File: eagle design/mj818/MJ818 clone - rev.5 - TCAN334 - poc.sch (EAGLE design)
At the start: 6 parts, among them J1 CAN, J2 Power Supply, J3 LED

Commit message: MJ818: confirmed pulldown resistor for rear LED PWM line (driver input side) is needed
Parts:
- removed R102: 10k, rcl:R-EU_R0402
- renumbered J1 to J103, J2 to J101, J3 to J102
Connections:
- removed net DIM_REAR: R102.2
- net GND: no longer R102.1
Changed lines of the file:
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@@
 <part name="SUPPLY12" library="Power_Symbols" library_urn="urn:adsk.eagle:library:16502351" deviceset="GND-BAR" device="" value="GND"/>
 <part name="SUPPLY13" library="Power_Symbols" library_urn="urn:adsk.eagle:library:16502351" deviceset="GND-BAR" device="" value="GND"/>
+<part name="R1" library="rcl" library_urn="urn:adsk.eagle:library:334" deviceset="R-EU_" device="R0402" package3d_urn="urn:adsk.eagle:package:23547/3" value="10k"/>
+<part name="SUPPLY1" library="Power_Symbols" library_urn="urn:adsk.eagle:library:16502351" deviceset="GND-BAR" device="" value="GND"/>
 </parts>
 <sheets>
@@
 <attribute name="VALUE" x="144.78" y="10.795" size="1.778" layer="96" align="center"/>
 </instance>
+<instance part="R1" gate="G$1" x="205.74" y="104.14" smashed="yes" rot="R90">
+<attribute name="NAME" x="208.28" y="104.14" size="1.778" layer="95"/>
+<attribute name="VALUE" x="208.28" y="101.6" size="1.778" layer="96"/>
+</instance>
+<instance part="SUPPLY1" gate="G$1" x="205.74" y="93.98" smashed="yes">
+<attribute name="VALUE" x="205.74" y="92.075" size="1.778" layer="96" align="center"/>
+</instance>
 </instances>
 <busses>
@@
 <net name="DIM_REAR" class="3">
 <segment>
-<wire x1="182.88" y1="109.22" x2="203.2" y2="109.22" width="0.1524" layer="91"/>
-<label x="203.2" y="109.22" size="1.778" layer="95" xref="yes"/>
+<wire x1="182.88" y1="109.22" x2="205.74" y2="109.22" width="0.1524" layer="91"/>
+<label x="218.44" y="109.22" size="1.778" layer="95" xref="yes"/>
 <pinref part="IC1" gate="G$1" pin="DIM"/>
+<pinref part="R1" gate="G$1" pin="2"/>
+<wire x1="205.74" y1="109.22" x2="218.44" y2="109.22" width="0.1524" layer="91"/>
+<junction x="205.74" y="109.22"/>
 </segment>
 </net>
@@
 <pinref part="IC1" gate="G$1" pin="FLTS"/>
 <pinref part="SUPPLY12" gate="G$1" pin="GND"/>
+</segment>
+<segment>
+<pinref part="R1" gate="G$1" pin="1"/>
+<pinref part="SUPPLY1" gate="G$1" pin="GND"/>
+<wire x1="205.74" y1="96.52" x2="205.74" y2="99.06" width="0.1524" layer="91"/>
 </segment>
 </net>
@@
 <part name="FRAME101" library="frames" library_urn="urn:adsk.eagle:library:229" deviceset="A3L-LOC" device="" value="MJ818"/>
 <part name="SUPPLY9" library="Power_Symbols" library_urn="urn:adsk.eagle:library:16502351" deviceset="GND-BAR" device="" value="GND"/>
-<part name="R102" library="rcl" library_urn="urn:adsk.eagle:library:334" deviceset="R-EU_" device="R0402" package3d_urn="urn:adsk.eagle:package:23547/3" value="10k"/>
-<part name="SUPPLY10" library="Power_Symbols" library_urn="urn:adsk.eagle:library:16502351" deviceset="GND-BAR" device="" value="GND"/>
-<part name="J2" library="con-amp" library_urn="urn:adsk.eagle:library:127" deviceset="MTA02-100" device="" package3d_urn="urn:adsk.eagle:package:8081649/1" value="Power Supply"/>
-<part name="J1" library="con-amp" library_urn="urn:adsk.eagle:library:127" deviceset="MTA02-100" device="" package3d_urn="urn:adsk.eagle:package:8081649/1" value="CAN"/>
-<part name="J3" library="con-amp" library_urn="urn:adsk.eagle:library:127" deviceset="MTA02-100" device="" package3d_urn="urn:adsk.eagle:package:8081649/1" value="LED"/>
+<part name="J101" library="con-amp" library_urn="urn:adsk.eagle:library:127" deviceset="MTA02-100" device="" package3d_urn="urn:adsk.eagle:package:8081649/1" value="Power Supply"/>
+<part name="J103" library="con-amp" library_urn="urn:adsk.eagle:library:127" deviceset="MTA02-100" device="" package3d_urn="urn:adsk.eagle:package:8081649/1" value="CAN"/>
+<part name="J102" library="con-amp" library_urn="urn:adsk.eagle:library:127" deviceset="MTA02-100" device="" package3d_urn="urn:adsk.eagle:package:8081649/1" value="LED"/>
 </parts>
 <sheets>
@@
 <text x="38.1" y="210.82" size="6.4516" layer="98" rot="R180" align="bottom-right">MJ8x8 - generic</text>
 <text x="203.2" y="170.18" size="6.4516" layer="94">???</text>
-<text x="205.74" y="137.16" size="6.4516" layer="94">???</text>
 <wire x1="255.27" y1="189.23" x2="257.175" y2="191.77" width="0.1524" layer="98"/>
 <wire x1="257.175" y1="191.77" x2="255.27" y2="191.77" width="0.1524" layer="98"/>
@@
 <attribute name="VALUE" x="223.52" y="130.175" size="1.778" layer="96" align="center"/>
 </instance>
-<instance part="R102" gate="G$1" x="203.2" y="144.78" smashed="yes" rot="R90">
-<attribute name="NAME" x="205.74" y="144.78" size="1.778" layer="95"/>
-<attribute name="VALUE" x="205.74" y="142.24" size="1.778" layer="96"/>
-</instance>
-<instance part="SUPPLY10" gate="G$1" x="203.2" y="134.62" smashed="yes">
-<attribute name="VALUE" x="203.2" y="132.715" size="1.778" layer="96" align="center"/>
-</instance>
-<instance part="J2" gate="G$1" x="60.96" y="119.38" smashed="yes" rot="R90">
+<instance part="J101" gate="G$1" x="60.96" y="119.38" smashed="yes" rot="R90">
 <attribute name="NAME" x="60.96" y="124.46" size="1.778" layer="95"/>
 <attribute name="VALUE" x="64.77" y="124.46" size="1.778" layer="96" rot="R90"/>
 </instance>
-<instance part="J1" gate="G$1" x="254" y="91.44" smashed="yes" rot="R270">
+<instance part="J103" gate="G$1" x="254" y="91.44" smashed="yes" rot="R270">
 <attribute name="NAME" x="254" y="96.52" size="1.778" layer="95"/>
 <attribute name="VALUE" x="250.19" y="86.36" size="1.778" layer="96" rot="R270"/>
 </instance>
-<instance part="J3" gate="G$1" x="248.92" y="190.5" smashed="yes" rot="MR90">
+<instance part="J102" gate="G$1" x="248.92" y="190.5" smashed="yes" rot="MR90">
 <attribute name="NAME" x="248.92" y="195.58" size="1.778" layer="95" rot="MR90"/>
 <attribute name="VALUE" x="245.11" y="195.58" size="1.778" layer="96" rot="MR90"/>
@@
 <pinref part="SUPPLY6" gate="G$1" pin="GND"/>
 <wire x1="66.04" y1="119.38" x2="63.5" y2="119.38" width="0.1524" layer="91"/>
-<pinref part="J2" gate="G$1" pin="1"/>
+<pinref part="J101" gate="G$1" pin="1"/>
 </segment>
 <segment>
@@
 <pinref part="SUPPLY9" gate="G$1" pin="GND"/>
 <wire x1="223.52" y1="134.62" x2="223.52" y2="137.16" width="0.1524" layer="91"/>
-</segment>
-<segment>
-<pinref part="R102" gate="G$1" pin="1"/>
-<pinref part="SUPPLY10" gate="G$1" pin="GND"/>
-<wire x1="203.2" y1="137.16" x2="203.2" y2="139.7" width="0.1524" layer="91"/>
 </segment>
 </net>
@@
 <portref moduleinst="REAR_LED_DRIVER" port="DIM_REAR"/>
 <wire x1="203.2" y1="149.86" x2="198.12" y2="149.86" width="0.1524" layer="91"/>
-<pinref part="R102" gate="G$1" pin="2"/>
-<junction x="203.2" y="149.86"/>
 </segment>
 </net>
@@
 <label x="243.84" y="187.96" size="1.778" layer="95" rot="R270"/>
 <portref moduleinst="BRAKE_LED_DRIVER" port="LED_CA"/>
-<pinref part="J3" gate="G$1" pin="1"/>
+<pinref part="J102" gate="G$1" pin="1"/>
 </segment>
 </net>
@@
 <wire x1="175.26" y1="154.94" x2="175.26" y2="193.04" width="0.1524" layer="91"/>
 <junction x="175.26" y="193.04"/>
-<pinref part="J2" gate="G$1" pin="2"/>
+<pinref part="J101" gate="G$1" pin="2"/>
 </segment>
 </net>
@@
 <portref moduleinst="BRAKE_LED_DRIVER" port="LED_AN"/>
 <label x="243.84" y="193.04" size="1.778" layer="95" rot="R90"/>
-<pinref part="J3" gate="G$1" pin="2"/>
+<pinref part="J102" gate="G$1" pin="2"/>
 </segment>
 </net>
@@
 <wire x1="246.38" y1="91.44" x2="251.46" y2="91.44" width="0.1524" layer="91"/>
 <label x="246.38" y="91.44" size="1.778" layer="95" rot="R180"/>
-<pinref part="J1" gate="G$1" pin="1"/>
+<pinref part="J103" gate="G$1" pin="1"/>
 </segment>
 </net>
@@
 </segment>
 <segment>
-<pinref part="J1" gate="G$1" pin="2"/>
+<pinref part="J103" gate="G$1" pin="2"/>
 <wire x1="251.46" y1="88.9" x2="246.38" y2="88.9" width="0.1524" layer="91"/>
 <label x="246.38" y="86.36" size="1.778" layer="95" rot="R180"/>

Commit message: board revision 5a: - removed CAN infra shutdown pin, since it is not needed
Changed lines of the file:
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@@
 <port name="DIM_REAR" side="top" coord="17.78" direction="out"/>
 <port name="DIM_BRAKE" side="top" coord="12.7" direction="out"/>
-<port name="!SHDN!" side="bottom" coord="-15.24" direction="out"/>
 </ports>
 <variantdefs>
@@
 <text x="167.64" y="119.38" size="1.778" layer="98" align="center-left">timer3 channel4</text>
 <text x="160.02" y="134.62" size="1.778" layer="98">GPIO</text>
-<text x="160.02" y="88.9" size="1.778" layer="98">GPIO</text>
+<text x="137.16" y="88.9" size="1.778" layer="98">GPIO</text>
 </plain>
 <instances>
@@
 <wire x1="129.54" y1="119.38" x2="149.86" y2="119.38" width="0.1524" layer="91"/>
 <pinref part="IC2" gate="G$1" pin="ADC_IN9,TSC_G3_IO3,TIM1_CH3N,TIM3_CH4,TIM14_CH1-PB1_15"/>
-</segment>
-</net>
-<net name="!SHDN!" class="0">
-<segment>
-<wire x1="129.54" y1="88.9" x2="149.86" y2="88.9" width="0.1524" layer="91"/>
-<label x="149.86" y="88.9" size="1.778" layer="95" xref="yes"/>
-<pinref part="IC2" gate="G$1" pin="EVENTOUT,TSC_G5_IO2,TIM3_CH1,TIM17_BKIN,SPI1_MISO,I2S1_MCK-PB4_25"/>
 </segment>
 </net>
@@
 <port name="RXCAN" side="left" coord="2.54" direction="out"/>
 <port name="!STBY!" side="left" coord="0" direction="in"/>
-<port name="!SHDN!" side="left" coord="-2.54" direction="in"/>
 </ports>
 <variantdefs>
@@
 <sheet>
 <plain>
-<text x="40.64" y="71.12" size="1.778" layer="97" rot="R180">internal pulldown</text>
+<text x="66.04" y="71.12" size="1.778" layer="97" rot="R180" align="top-left">internal pulldown</text>
 <text x="40.64" y="68.58" size="1.778" layer="97" rot="R180">internal pulldown</text>
 </plain>
@@
 <wire x1="142.24" y1="104.14" x2="142.24" y2="101.6" width="0.1524" layer="91"/>
 <label x="142.24" y="101.6" size="0.8128" layer="95"/>
-</segment>
-</net>
-<net name="!SHDN!" class="0">
-<segment>
-<pinref part="IC1" gate="G$1" pin="5_SHDN"/>
-<wire x1="68.58" y1="71.12" x2="50.8" y2="71.12" width="0.1524" layer="91"/>
-<label x="50.8" y="71.12" size="1.778" layer="95" rot="R180" xref="yes"/>
 </segment>
 </net>
@@
 </segment>
 </net>
-<net name="!SHDN!" class="0">
-<segment>
-<portref moduleinst="CAN_INFRA" port="!SHDN!"/>
-<wire x1="172.72" y1="83.82" x2="165.1" y2="83.82" width="0.1524" layer="91"/>
-<wire x1="165.1" y1="83.82" x2="165.1" y2="106.68" width="0.1524" layer="91"/>
-<portref moduleinst="STM32F04" port="!SHDN!"/>
-</segment>
-</net>

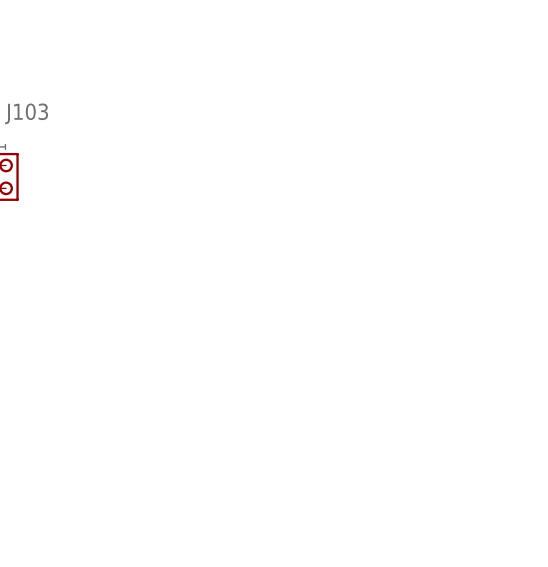
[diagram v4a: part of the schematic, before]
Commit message: - updated mj8x8 template board and schematic with previous changes - added TODOs for mj808/818/828 boards (rerouting, mostly)
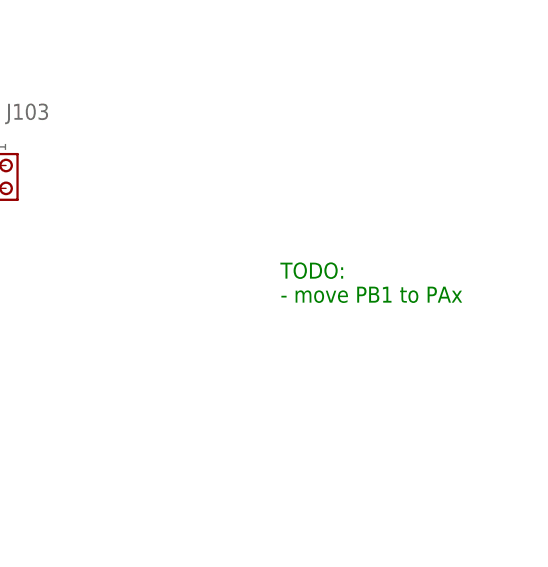
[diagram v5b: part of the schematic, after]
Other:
- note added: "TODO: - move PB1 to PAx"
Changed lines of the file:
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@@
 <wire x1="255.27" y1="191.77" x2="255.27" y2="193.04" width="0.1524" layer="98"/>
 <wire x1="253.365" y1="189.23" x2="257.175" y2="189.23" width="0.1524" layer="98"/>
+<text x="284.48" y="76.2" size="1.778" layer="91">TODO:
+- move PB1 to PAx</text>
 </plain>
 <moduleinsts>

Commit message: - unified values of passive elements to a common format
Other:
- note added: "9x LED: Vf = 2.0V 4.5cd or more"
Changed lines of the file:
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@@
 <parts>
 <part name="IC2" library="LDK320 5V LDO" deviceset="LDK320" device="SOT-23-5L" value="LDK320AM33R"/>
-<part name="C2" library="rcl" library_urn="urn:adsk.eagle:library:334" deviceset="C-EU" device="C0402" package3d_urn="urn:adsk.eagle:package:23626/2" value="1μF / 10V"/>
-<part name="C7" library="rcl" library_urn="urn:adsk.eagle:library:334" deviceset="C-EU" device="C0402" package3d_urn="urn:adsk.eagle:package:23626/2" value="1μF"/>
+<part name="C2" library="rcl" library_urn="urn:adsk.eagle:library:334" deviceset="C-EU" device="C0402" package3d_urn="urn:adsk.eagle:package:23626/2" value="1uF / 10V"/>
+<part name="C7" library="rcl" library_urn="urn:adsk.eagle:library:334" deviceset="C-EU" device="C0402" package3d_urn="urn:adsk.eagle:package:23626/2" value="1uF / 10V"/>
 <part name="POWER_3V3" library="frames" library_urn="urn:adsk.eagle:library:229" deviceset="DINA5_L" device="" value="POWER_3V3"/>
 <part name="SUPPLY1" library="Power_Symbols" library_urn="urn:adsk.eagle:library:16502351" deviceset="GND-BAR" device="" value="GND"/>
@@
 <part name="IC2" library="STM32F042G6" deviceset="STM32F042G6" device="" value="STM32F042G6U6"/>
 <part name="SUPPLY1" library="Power_Symbols" library_urn="urn:adsk.eagle:library:16502351" deviceset="GND-BAR" device="" value="GND"/>
-<part name="C1" library="rcl" library_urn="urn:adsk.eagle:library:334" deviceset="C-EU" device="C0402" package3d_urn="urn:adsk.eagle:package:23626/2" value="0.1u"/>
+<part name="C1" library="rcl" library_urn="urn:adsk.eagle:library:334" deviceset="C-EU" device="C0402" package3d_urn="urn:adsk.eagle:package:23626/2" value="0.1uF / 10V"/>
 <part name="SUPPLY2" library="Power_Symbols" library_urn="urn:adsk.eagle:library:16502351" deviceset="GND-BAR" device="" value="GND"/>
-<part name="C4" library="rcl" library_urn="urn:adsk.eagle:library:334" deviceset="C-EU" device="C0402" package3d_urn="urn:adsk.eagle:package:23626/2" value="1u"/>
+<part name="C4" library="rcl" library_urn="urn:adsk.eagle:library:334" deviceset="C-EU" device="C0402" package3d_urn="urn:adsk.eagle:package:23626/2" value="1uF / 10V"/>
 <part name="SUPPLY6" library="Power_Symbols" library_urn="urn:adsk.eagle:library:16502351" deviceset="GND-BAR" device="" value="GND"/>
-<part name="C5" library="rcl" library_urn="urn:adsk.eagle:library:334" deviceset="C-EU" device="C0402" package3d_urn="urn:adsk.eagle:package:23626/2" value="0.1u"/>
+<part name="C5" library="rcl" library_urn="urn:adsk.eagle:library:334" deviceset="C-EU" device="C0402" package3d_urn="urn:adsk.eagle:package:23626/2" value="0.1uF / 10V"/>
 <part name="SUPPLY7" library="Power_Symbols" library_urn="urn:adsk.eagle:library:16502351" deviceset="GND-BAR" device="" value="GND"/>
-<part name="C7" library="rcl" library_urn="urn:adsk.eagle:library:334" deviceset="C-EU" device="C0402" package3d_urn="urn:adsk.eagle:package:23626/2" value="0.1u"/>
+<part name="C7" library="rcl" library_urn="urn:adsk.eagle:library:334" deviceset="C-EU" device="C0402" package3d_urn="urn:adsk.eagle:package:23626/2" value="0.1uF / 10V"/>
 <part name="SUPPLY9" library="Power_Symbols" library_urn="urn:adsk.eagle:library:16502351" deviceset="GND-BAR" device="" value="GND"/>
 <part name="STM32_MICROCONTROLLER" library="frames" library_urn="urn:adsk.eagle:library:229" deviceset="A4L-LOC" device="" value="STM32_MICROCONTROLLER"/>
@@
 <part name="SUPPLY1" library="Power_Symbols" library_urn="urn:adsk.eagle:library:16502351" deviceset="GND-BAR" device="" value="GND"/>
 <part name="R5" library="rcl" library_urn="urn:adsk.eagle:library:334" deviceset="R-EU_" device="R0805" package3d_urn="urn:adsk.eagle:package:23553/2" value="60"/>
-<part name="C5" library="rcl" library_urn="urn:adsk.eagle:library:334" deviceset="C-EU" device="C0402" package3d_urn="urn:adsk.eagle:package:23626/2" value="0.1μF"/>
+<part name="C5" library="rcl" library_urn="urn:adsk.eagle:library:334" deviceset="C-EU" device="C0402" package3d_urn="urn:adsk.eagle:package:23626/2" value="0.1uF / 10V"/>
 <part name="SUPPLY2" library="Power_Symbols" library_urn="urn:adsk.eagle:library:16502351" deviceset="GND-BAR" device="" value="GND"/>
 <part name="SUPPLY3" library="Power_Symbols" library_urn="urn:adsk.eagle:library:16502351" deviceset="GND-BAR" device="" value="GND"/>
 <part name="CAN_INFRA" library="frames" library_urn="urn:adsk.eagle:library:229" deviceset="DINA5_L" device="" value="CAN_INFRA"/>
 <part name="IC1" library="TCAN33x - 3.3V CAN Transciever" deviceset="CAN33X" device="" value="TCAN334"/>
-<part name="C1" library="rcl" library_urn="urn:adsk.eagle:library:334" deviceset="C-EU" device="C0402" package3d_urn="urn:adsk.eagle:package:23626/2" value="47nF"/>
+<part name="C1" library="rcl" library_urn="urn:adsk.eagle:library:334" deviceset="C-EU" device="C0402" package3d_urn="urn:adsk.eagle:package:23626/2" value="47nF / 10V"/>
 <part name="SUPPLY4" library="Power_Symbols" library_urn="urn:adsk.eagle:library:16502351" deviceset="GND-BAR" device="" value="GND"/>
 <part name="R1" library="rcl" library_urn="urn:adsk.eagle:library:334" deviceset="R-EU_" device="R0805" package3d_urn="urn:adsk.eagle:package:23553/2" value="60"/>
@@
 </variantdefs>
 <parts>
-<part name="C6" library="rcl" library_urn="urn:adsk.eagle:library:334" deviceset="C-EU" device="C0402" package3d_urn="urn:adsk.eagle:package:23626/2" value="1μF / 10V"/>
+<part name="C6" library="rcl" library_urn="urn:adsk.eagle:library:334" deviceset="C-EU" device="C0402" package3d_urn="urn:adsk.eagle:package:23626/2" value="1uF / 10V"/>
 <part name="D1" library="diode" library_urn="urn:adsk.eagle:library:210" deviceset="DIODE-" device="SOD123" package3d_urn="urn:adsk.eagle:package:43420/1" value="PMEG2010ER,115"/>
 <part name="IC6" library="MAX16820 LED Driver, constant current" deviceset="MAX16820" device="" value="MAX16820"/>
@@
 <part name="IC1" library="MAX16839 LED Driver, constant current" deviceset="MAX16839" device="" value="MAX16839 "/>
 <part name="R2" library="rcl" library_urn="urn:adsk.eagle:library:334" deviceset="R-EU_" device="R0603" package3d_urn="urn:adsk.eagle:package:23555/3" value="10R/0.5W"/>
-<part name="C1" library="rcl" library_urn="urn:adsk.eagle:library:334" deviceset="C-EU" device="C0402" package3d_urn="urn:adsk.eagle:package:23626/2" value="1μF"/>
+<part name="C1" library="rcl" library_urn="urn:adsk.eagle:library:334" deviceset="C-EU" device="C0402" package3d_urn="urn:adsk.eagle:package:23626/2" value="1uF / 10V"/>
 <part name="SUPPLY9" library="Power_Symbols" library_urn="urn:adsk.eagle:library:16502351" deviceset="GND-BAR" device="" value="GND"/>
 <part name="SUPPLY10" library="Power_Symbols" library_urn="urn:adsk.eagle:library:16502351" deviceset="GND-BAR" device="" value="GND"/>
@@
 <sheet>
 <plain>
+<text x="55.88" y="86.36" size="1.778" layer="97">9x LED:
+Vf = 2.0V
+4.5cd or more</text>
 </plain>
 <instances>

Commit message: - validated that pulldown for MAX16820 dim line is not needed on MJ808/818
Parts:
- removed R101: 10k, rcl:R-EU_R0402
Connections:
- removed net DIM_BRAKE: R101.2
- net GND: no longer R101.1
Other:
- note removed: "???"
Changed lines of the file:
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@@
 <part name="SUPPLY6" library="Power_Symbols" library_urn="urn:adsk.eagle:library:16502351" deviceset="GND-BAR" device="" value="GND"/>
 <part name="SUPPLY7" library="Power_Symbols" library_urn="urn:adsk.eagle:library:16502351" deviceset="GND-BAR" device="" value="GND"/>
-<part name="R101" library="rcl" library_urn="urn:adsk.eagle:library:334" deviceset="R-EU_" device="R0402" package3d_urn="urn:adsk.eagle:package:23547/3" value="10k"/>
-<part name="SUPPLY8" library="Power_Symbols" library_urn="urn:adsk.eagle:library:16502351" deviceset="GND-BAR" device="" value="GND"/>
 <part name="FRAME101" library="frames" library_urn="urn:adsk.eagle:library:229" deviceset="A3L-LOC" device="" value="MJ818"/>
 <part name="SUPPLY9" library="Power_Symbols" library_urn="urn:adsk.eagle:library:16502351" deviceset="GND-BAR" device="" value="GND"/>
@@
 <wire x1="33.02" y1="48.26" x2="271.78" y2="48.26" width="0.1524" layer="98" style="dashdot"/>
 <text x="38.1" y="210.82" size="6.4516" layer="98" rot="R180" align="bottom-right">MJ8x8 - generic</text>
-<text x="203.2" y="170.18" size="6.4516" layer="94">???</text>
 <wire x1="255.27" y1="189.23" x2="257.175" y2="191.77" width="0.1524" layer="98"/>
 <wire x1="257.175" y1="191.77" x2="255.27" y2="191.77" width="0.1524" layer="98"/>
@@
 <instance part="SUPPLY7" gate="G$1" x="149.86" y="165.1" smashed="yes" rot="R90">
 <attribute name="VALUE" x="151.765" y="165.1" size="1.778" layer="96" rot="R90" align="center"/>
-</instance>
-<instance part="R101" gate="G$1" x="198.12" y="182.88" smashed="yes" rot="R90">
-<attribute name="NAME" x="200.66" y="182.88" size="1.778" layer="95"/>
-<attribute name="VALUE" x="200.66" y="180.34" size="1.778" layer="96"/>
-</instance>
-<instance part="SUPPLY8" gate="G$1" x="198.12" y="172.72" smashed="yes">
-<attribute name="VALUE" x="198.12" y="170.815" size="1.778" layer="96" align="center"/>
 </instance>
 <instance part="FRAME101" gate="G$1" x="0" y="0" smashed="yes">
@@
 </segment>
 <segment>
-<pinref part="R101" gate="G$1" pin="1"/>
-<pinref part="SUPPLY8" gate="G$1" pin="GND"/>
-<wire x1="198.12" y1="175.26" x2="198.12" y2="177.8" width="0.1524" layer="91"/>
-</segment>
-<segment>
 <portref moduleinst="REAR_LED_DRIVER" port="GND"/>
 <pinref part="SUPPLY9" gate="G$1" pin="GND"/>
@@
 <portref moduleinst="BRAKE_LED_DRIVER" port="DIM_BRAKE"/>
 <wire x1="193.04" y1="137.16" x2="193.04" y2="187.96" width="0.1524" layer="91"/>
-<wire x1="193.04" y1="187.96" x2="198.12" y2="187.96" width="0.1524" layer="91"/>
 <label x="193.04" y="157.48" size="1.778" layer="95" rot="R90"/>
-<pinref part="R101" gate="G$1" pin="2"/>
-<wire x1="198.12" y1="187.96" x2="203.2" y2="187.96" width="0.1524" layer="91"/>
-<junction x="198.12" y="187.96"/>
+<wire x1="193.04" y1="187.96" x2="203.2" y2="187.96" width="0.1524" layer="91"/>
 </segment>
 </net>
